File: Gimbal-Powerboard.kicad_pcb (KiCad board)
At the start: 2 copper layers, 166 parts, among them Q1 Q_PMOS_GDS, Q2 Q_PMOS_GDS, Q3 SI4116DY, Q4 SI4116DY, Q5 SI4116DY, Q6 SI4116DY, Q7 SI4116DY, Q8 SI4116DY, U1 DRV8301, U2 NUP4201MR6, U27 2P2T_Switch, U3 LAUNCHXL-F28069M_Launchpad_J1, U4 ACS711, U5 Molex_SL-3, U6 Molex_SL-5, U7 ACS711, U8 MAX_3232

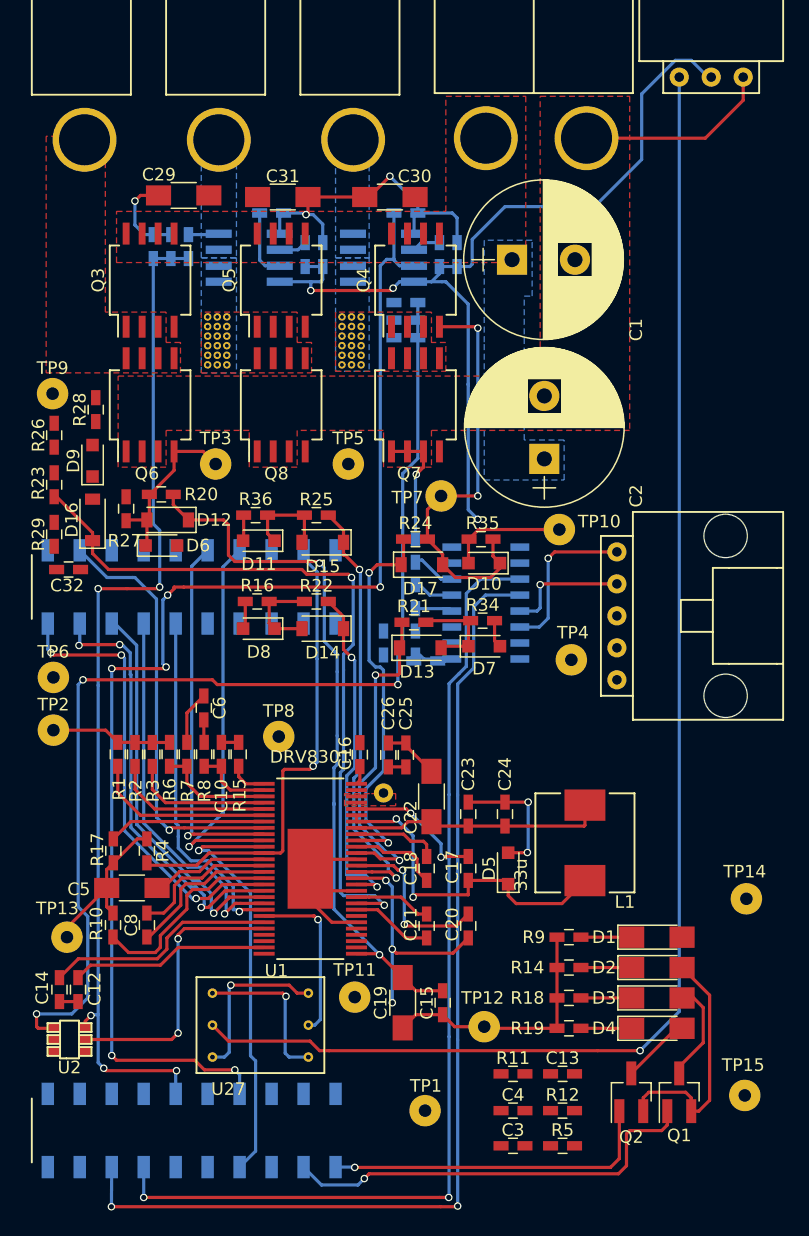
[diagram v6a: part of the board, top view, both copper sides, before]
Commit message: Finished all routing
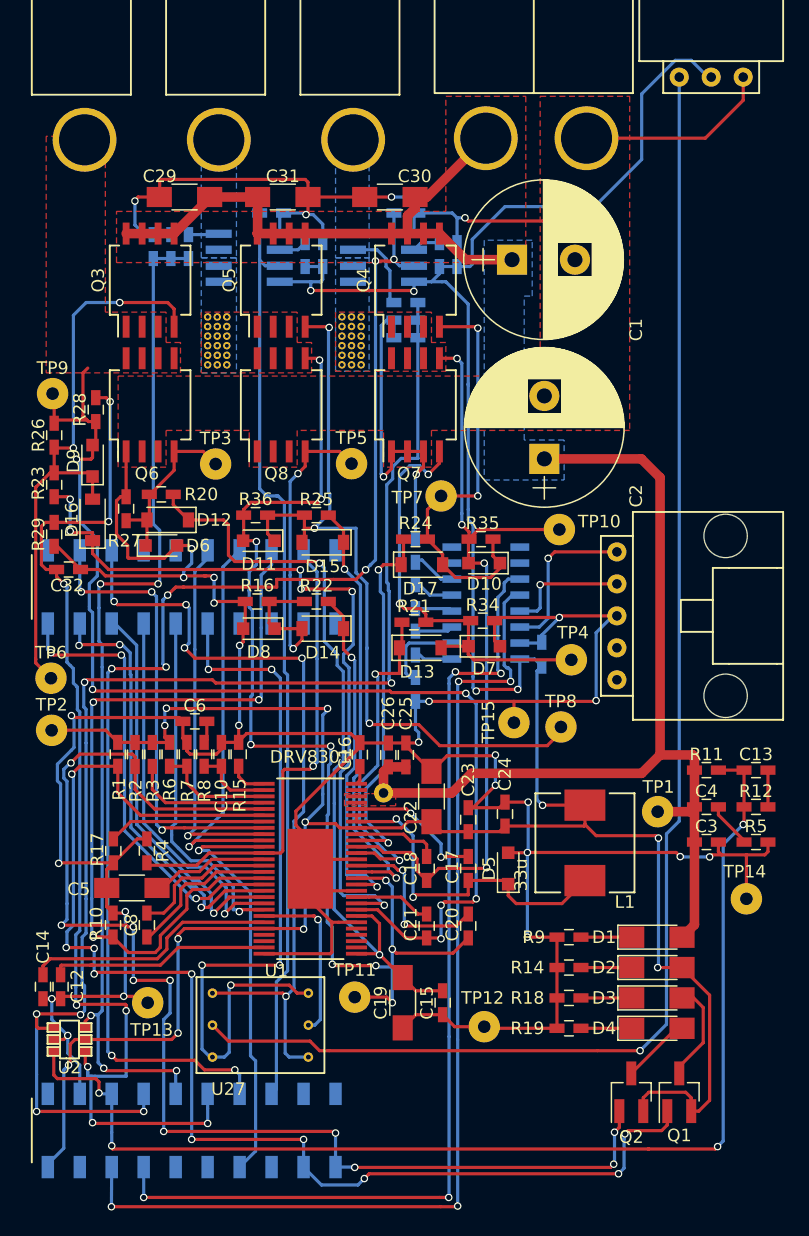
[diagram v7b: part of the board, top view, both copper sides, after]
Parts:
- moved TP15 34.8 mm to (151.6, 91.0)
- moved TP1 30.1 mm to (163.0, 98.1)
- moved C13 28.6 mm to (170.8, 94.8)
- moved R11 28.6 mm to (166.9, 94.8)
- moved C3 28.6 mm to (166.9, 100.5)
- moved C4 28.6 mm to (166.9, 97.7)
- moved R12 28.6 mm to (170.8, 97.7)
- moved R5 28.6 mm to (170.8, 100.5)
- moved TP8 22.4 mm to (155.3, 91.4)
- moved C35 9.24 mm to (153.8, 85.6), turned to 90 degrees
- moved TP13 8.26 mm to (122.5, 113.3)
- moved C42 4.47 mm to (143.8, 88.4)
- moved C12 1.40 mm to (115.6, 112.0)
- moved C14 1.33 mm to (114.2, 112.0)
- moved C6 1.28 mm to (126.2, 90.9), turned to 0 degrees
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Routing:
- net GND: track 133.7 -> 386.5 mm, vias 6 -> 29
- net 12VACT: track 1.40 -> 125.7 mm
- net VCC: track 145.4 -> 254.8 mm, vias 5 -> 15
- net 12VACTSENSE: track 0.00 -> 93.1 mm, vias 0 -> 4
- net MTC: track 6.51 -> 93.7 mm, vias 0 -> 6
- net CSENSE: track 0.00 -> 86.3 mm, vias 0 -> 8
- net SH_B: track 21.1 -> 90.0 mm, vias 3 -> 10
- net CURRENTSENSEB: track 5.53 -> 73.7 mm
- net NOCTW: track 39.3 -> 100.9 mm, vias 1 -> 10
- net Net-(D11-Pad1): track 7.43 -> 62.8 mm, vias 0 -> 3
- net NFAULT: track 48.5 -> 103.0 mm, vias 1 -> 10
- net INL_C/PWM_IN_2: track 13.2 -> 64.2 mm, vias 1 -> 5
- net Net-(D16-Pad2): track 0.00 -> 46.9 mm, vias 0 -> 2
- net SH_A: track 16.7 -> 63.5 mm, vias 0 -> 4
- net EN_GATE: track 16.1 -> 62.9 mm, vias 0 -> 3
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
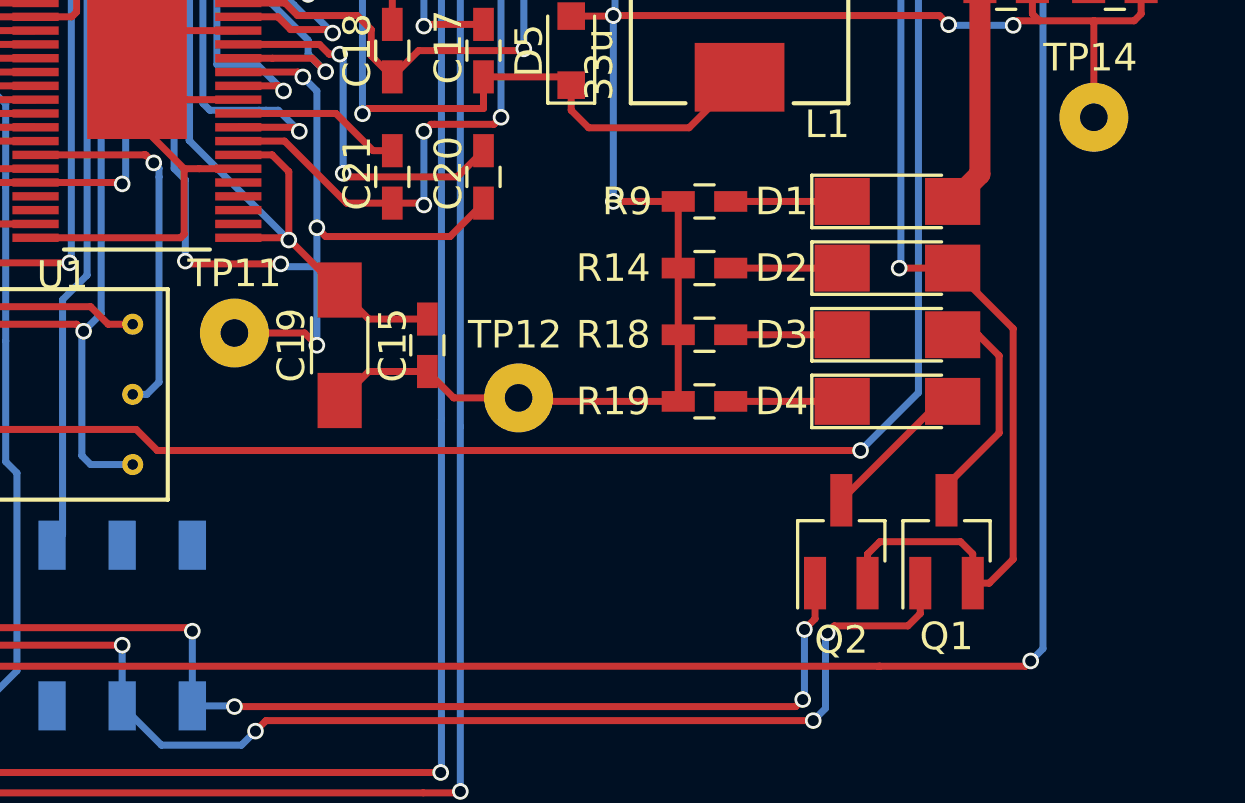
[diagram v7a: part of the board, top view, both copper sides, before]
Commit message: Added silkscreen for indicator LEDs and 2P2T switch
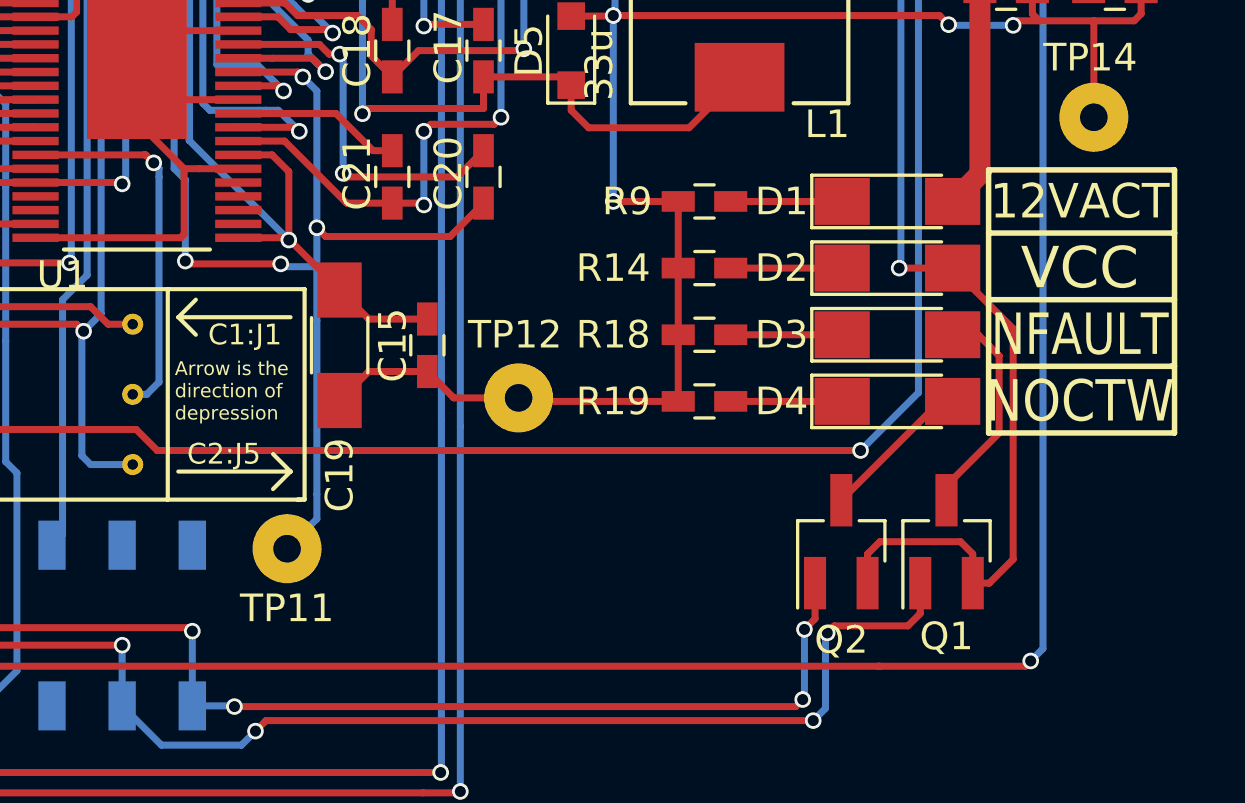
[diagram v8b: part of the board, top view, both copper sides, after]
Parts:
- moved TP11 8.04 mm to (140.8, 120.7)
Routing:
- net SH_B: track 90.0 -> 94.7 mm, vias 10 -> 9
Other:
- board text added: "12VACT"
- board text added: "Arrow is the direction of depression"
- board text added: "C1:J1"
- board text added: "C2:J5"
- board text added: "NFAULT"
- board text added: "NOCTW"
- board text added: "VCC"
